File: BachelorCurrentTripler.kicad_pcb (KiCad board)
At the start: 4 copper layers, 81.8 x 81.3 mm, 50 parts, among them J1 Conn_01x07_Pin, J2 Conn_01x01_Pin, J3 Conn_01x01_Pin, J4 Conn_01x04_Socket, J5 Conn_01x01_Pin, Q13 C2M0025120D, Q14 C2M0025120D, Q15 C2M0025120D, Q16 C2M0025120D, Q7 C2M0025120D, Q8 C2M0025120D, U1 STDriveG600, U2 STDriveG600, U3 STDriveG600

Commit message: vias
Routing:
- net /PhaseA/AOUT: track 39.5 -> 47.2 mm
- net GND: track 42.7 -> 45.0 mm, vias 109 -> 105
- net /PhaseC/COUT: track 69.0 -> 66.8 mm
- net Net-(U3-BOOT): track 0.00 -> 2.24 mm
- net /PhaseB/PVCC: track 10.3 -> 11.0 mm

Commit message: local restore changes
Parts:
- C12, C18, C6: value 100u -> 47u; footprint Capacitor_SMD:C_Elec_6.3x7.7 -> easyeda:CAP-SMD_BD6.3-L6.6-W6.6-LS7.3-FD
- C13, C19, C7: footprint Capacitor_SMD:C_Elec_6.3x7.7 -> easyeda:CAP-SMD_BD8.0-L8.3-W8.3-LS9.2-FD-H10.5
- moved C18 1.71 mm to (134.0, 120.5)
- moved C7 1.44 mm to (150.7, 80.0)
- moved C13 1.31 mm to (150.5, 103.5)
- moved C6 0.86 mm to (141.2, 72.8)
- moved C12 0.68 mm to (141.8, 97.6)
- moved R17 0.42 mm to (129.4, 133.0)
- moved R18 0.42 mm to (129.4, 135.5)
- moved C14 0.42 mm to (122.3, 138.5)
- moved C15 0.42 mm to (115.3, 131.5)
- moved R19 0.42 mm to (109.8, 129.5)
- moved C16 0.42 mm to (123.8, 124.0)
- moved C17 0.42 mm to (146.8, 135.5)
- moved Q15 0.42 mm to (138.4, 128.2)
- moved Q16 0.42 mm to (138.4, 135.2)
- moved R14 0.42 mm to (117.1, 138.2)
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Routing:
- net /PhaseA/AOUT: track 47.2 -> 38.8 mm
- net /PhaseB/BOUT: track 47.0 -> 38.7 mm
- net /PhaseC/COUT: track 66.8 -> 58.5 mm
- net +48V: vias 70 -> 134
- added copper zone on In2.Cu, net +12V
- added copper zone on In2.Cu, net +48V
- added copper zone on B.Cu, net GND
- added copper zone on F.Cu, net GND
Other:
- board size 81.8 x 81.3 mm -> 81.8 x 77.8 mm
- board text added: "Stor kondensator mellem 48V og GND men også 12V og GND"
- board text added: "byt"
- board text added: "kør ikke strøm under"

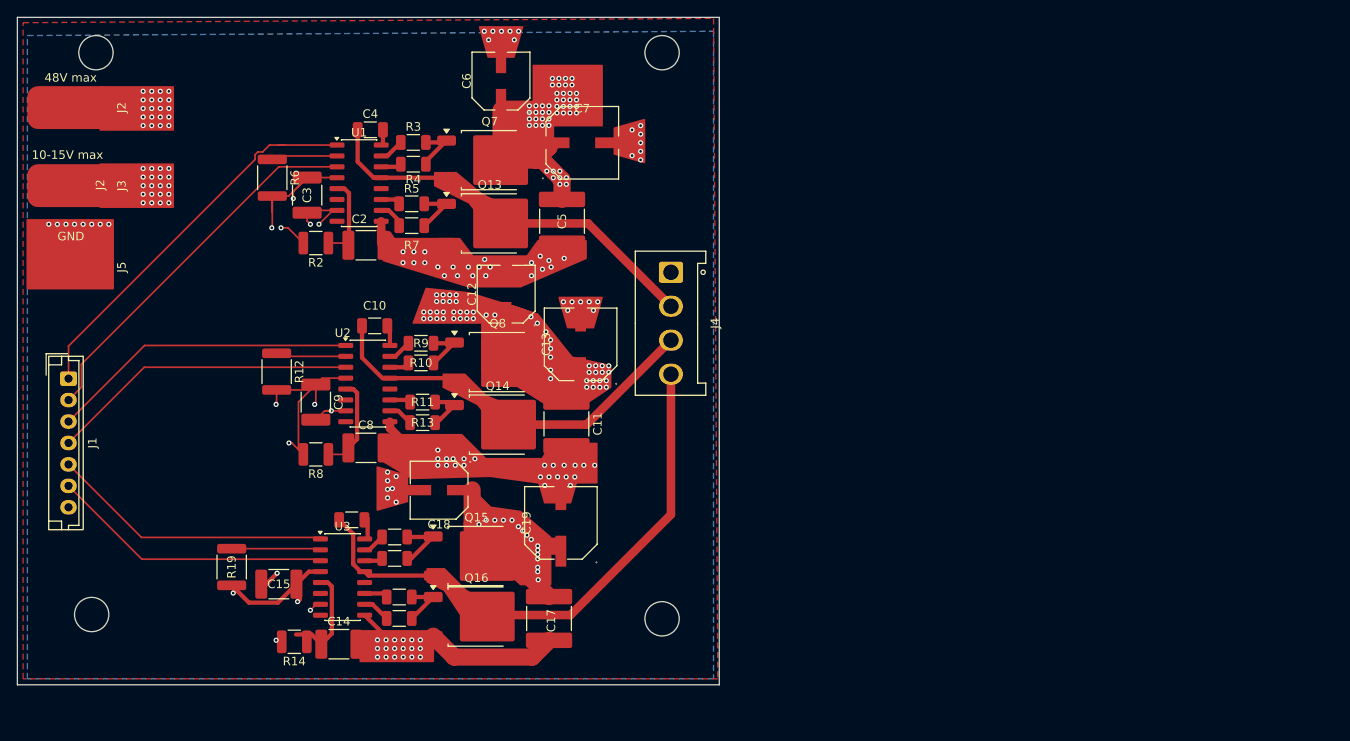
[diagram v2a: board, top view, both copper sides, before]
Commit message: Updates to Secondary side for PCB
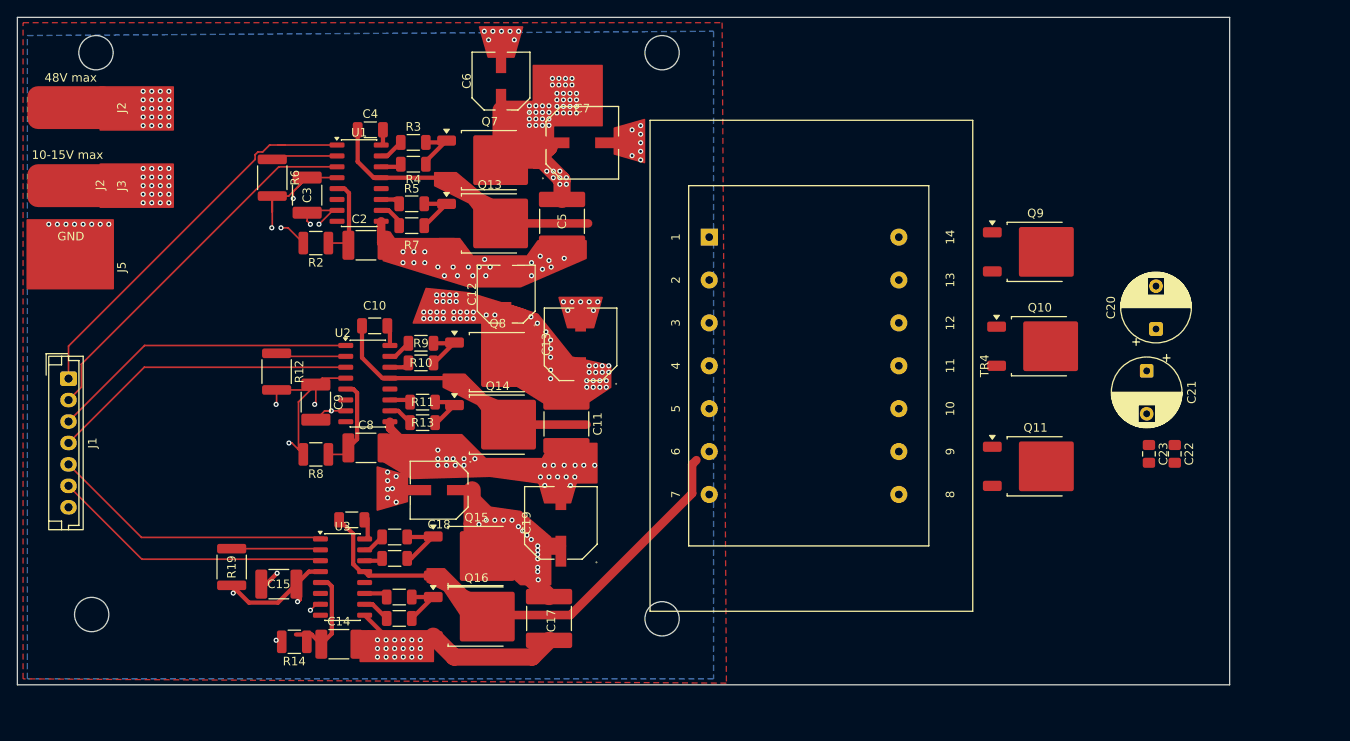
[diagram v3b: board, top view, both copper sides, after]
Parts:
- removed J4: Conn_01x04_Socket, Connector_Hirose:Hirose_DF63M-4P-3.96DSA_1x04_P3.96mm_Vertical
- added C20: 220u, Capacitor_THT:CP_Radial_D8.0mm_P5.00mm, F.Cu at (217.6, 101.7)
- added C21: 100u, Capacitor_THT:CP_Radial_D8.0mm_P5.00mm, F.Cu at (216.5, 106.6)
- added C22: 22u, Capacitor_SMD:C_0805_2012Metric_Pad1.18x1.45mm_HandSolder, F.Cu at (219.8, 116.3)
- added C23: 1u, Capacitor_SMD:C_0805_2012Metric_Pad1.18x1.45mm_HandSolder, F.Cu at (216.8, 116.3)
- added Q10: STD7NK40Z, Package_TO_SOT_SMD:TO-252-2, F.Cu at (204.0, 103.7)
- added Q11: STD7NK40Z, Package_TO_SOT_SMD:TO-252-2, F.Cu at (203.5, 117.7)
- added Q9: STD7NK40Z, Package_TO_SOT_SMD:TO-252-2, F.Cu at (203.5, 92.7)
- added TR4: TEZ16.0-D-1, Transformer_THT:Transformer_Breve_TEZ-47x57, F.Cu at (157.6, 91.0)
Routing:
- net /PhaseB/BOUT: track 38.7 -> 24.8 mm
- net /PhaseA/AOUT: track 38.8 -> 25.2 mm
- net /PhaseC/COUT: track 58.5 -> 49.7 mm
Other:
- board size 81.8 x 77.8 mm -> 141.3 x 77.8 mm

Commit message: all små komponenter er nu 0805, og jeg har fixet strømmen under kondensatorerene, mangler kun at bytte rundt på 12Vin og GND
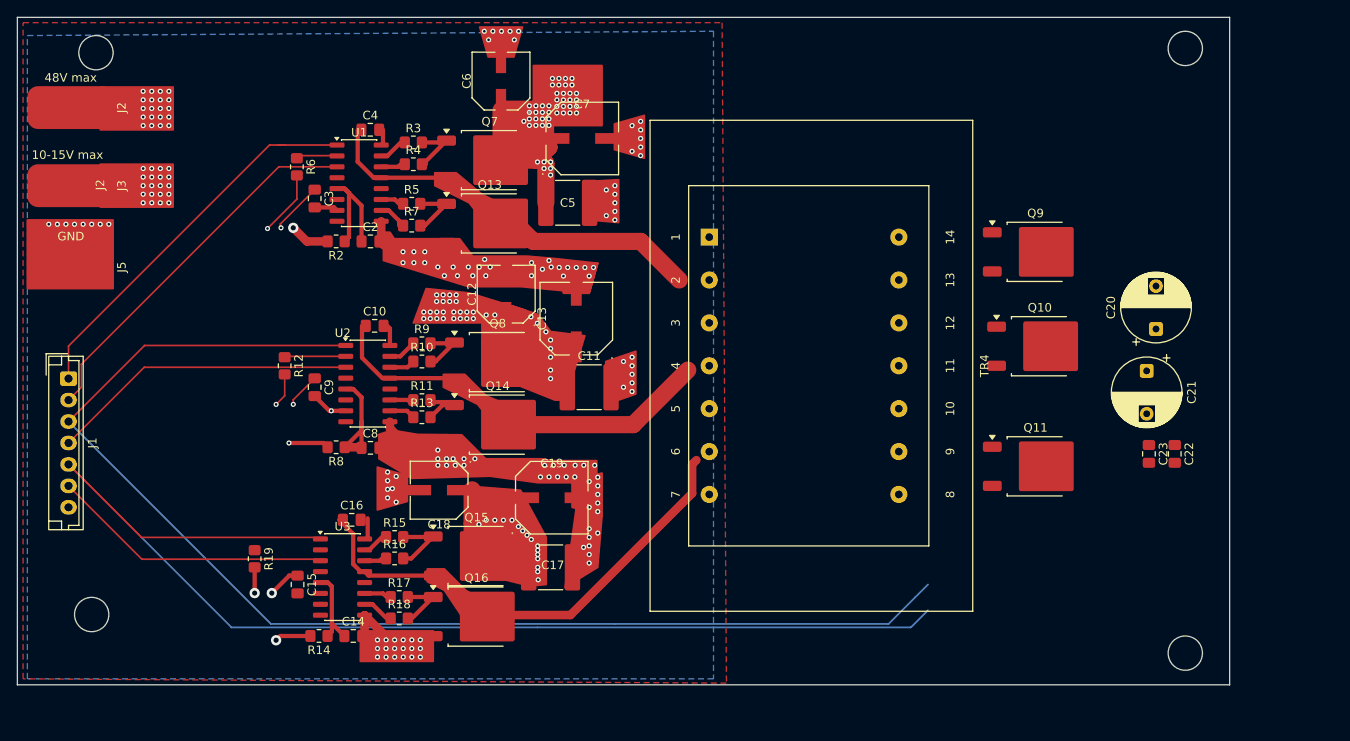
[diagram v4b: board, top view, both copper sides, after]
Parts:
- C10, C16, C4: footprint Capacitor_SMD:C_1206_3216Metric -> Capacitor_SMD:C_0805_2012Metric_Pad1.18x1.45mm_HandSolder
- C14, C15, C2, C3, C8, C9: footprint Capacitor_SMD:C_1812_4532Metric -> Capacitor_SMD:C_0805_2012Metric_Pad1.18x1.45mm_HandSolder
- R10, R11, R13, R15, R16, R17, R18, R3, R4, R5, R7, R9: footprint Resistor_SMD:R_1206_3216Metric -> Resistor_SMD:R_0805_2012Metric_Pad1.20x1.40mm_HandSolder
- R12, R19, R6: footprint Resistor_SMD:R_1812_4532Metric -> Resistor_SMD:R_0805_2012Metric_Pad1.20x1.40mm_HandSolder
- R14, R2, R8: footprint Resistor_SMD:R_1210_3225Metric -> Resistor_SMD:R_0805_2012Metric_Pad1.20x1.40mm_HandSolder
- moved C17 5.96 mm to (147.0, 129.5), turned to 0 degrees
- moved C11 5.03 mm to (151.5, 108.5), turned to 0 degrees
- moved R6 3.14 mm to (117.4, 82.8)
- moved C19 3.12 mm to (147.1, 121.4), turned to 0 degrees
- moved C13 3.04 mm to (150.0, 100.5)
- moved R14 2.96 mm to (120.0, 137.5)
- moved R19 2.85 mm to (112.5, 128.5)
- moved R8 2.51 mm to (122.0, 115.5)
- moved R2 2.37 mm to (122.0, 91.5)
- moved C5 2.25 mm to (149.0, 87.0), turned to 0 degrees
- moved C15 2.18 mm to (117.5, 131.5), turned to -90 degrees
- moved C14 1.93 mm to (124.0, 137.5)
- moved C9 1.74 mm to (119.5, 108.5)
- moved R12 1.16 mm to (116.0, 106.0)
- moved C3 0.97 mm to (119.5, 86.5)
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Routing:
- net /PhaseB/BLIN: track 36.0 -> 147.9 mm
- net /PhaseC/CLIN: track 33.3 -> 142.2 mm
- net +12V: track 180.5 -> 153.4 mm
- net GND: track 45.0 -> 22.0 mm, vias 105 -> 125
- net +48V: track 208.7 -> 192.1 mm, vias 134 -> 117
- net /PhaseB/BOUT: track 24.8 -> 39.2 mm
- net /PhaseA/AOUT: track 25.2 -> 38.5 mm
- net Net-(U3-SD): track 10.4 -> 0.19 mm
- net /PhaseA/PVCC: track 10.2 -> 14.4 mm
- net /PhaseB/PVCC: track 11.0 -> 14.1 mm
- net Net-(U1-SD): track 7.72 -> 4.82 mm
- net /PhaseC/PVCC: track 12.2 -> 9.57 mm
- net Net-(U2-HOFF): track 2.37 -> 3.01 mm
- net Net-(Q8-G): track 6.00 -> 6.63 mm
- net Net-(U2-HON): track 2.79 -> 3.36 mm
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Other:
- outline, holes or cut-outs redrawn

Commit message: nu er vi meget tættere på, den 3 fasede transformer er placeret og interegeret korrekt, sekundær siden er sat, spoler og mosfets, ved ikke om det er det rigtige at gøre men sådan er det jo
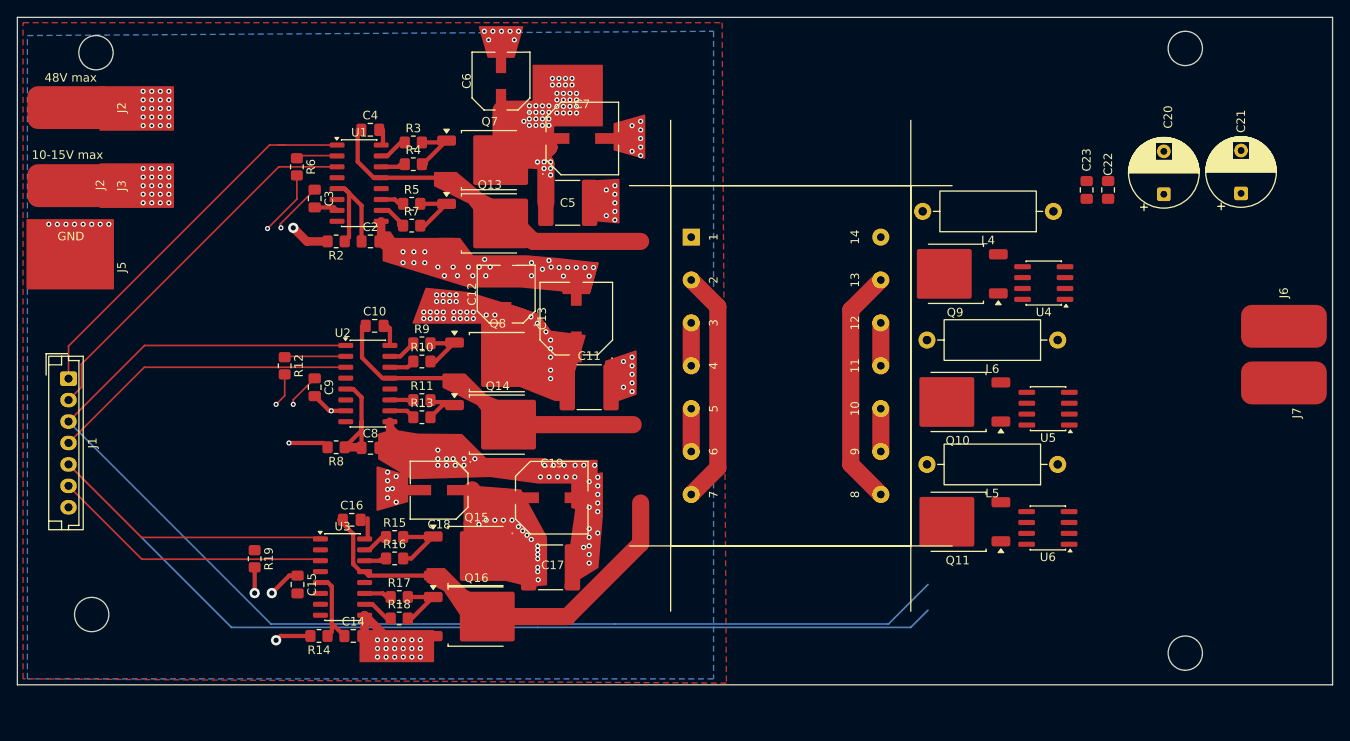
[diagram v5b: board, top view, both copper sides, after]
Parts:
- removed TR4: TEZ16.0-D-1, Transformer_THT:Transformer_Breve_TEZ-47x57
- added J6: Conn_01x01_Pin, Connector_Wire:SolderWirePad_1x01_SMD_5x10mm, F.Cu at (232.5, 101.4)
- added J7: Conn_01x01_Pin, Connector_Wire:SolderWirePad_1x01_SMD_5x10mm, F.Cu at (232.5, 108.0)
- added L4: L, Inductor_THT:L_Axial_L11.0mm_D4.5mm_P15.24mm_Horizontal_Fastron_MECC, F.Cu at (205.6, 88.0)
- added L5: L, Inductor_THT:L_Axial_L11.0mm_D4.5mm_P15.24mm_Horizontal_Fastron_MECC, F.Cu at (206.1, 117.5)
- added L6: L, Inductor_THT:L_Axial_L11.0mm_D4.5mm_P15.24mm_Horizontal_Fastron_MECC, F.Cu at (206.1, 103.0)
- added U4: FAN3268, Package_SO:SOIC-8_3.9x4.9mm_P1.27mm, F.Cu at (204.5, 96.4)
- added U5: FAN3268, Package_SO:SOIC-8_3.9x4.9mm_P1.27mm, F.Cu at (205.0, 111.0)
- added U6: FAN3268, Package_SO:SOIC-8_3.9x4.9mm_P1.27mm, F.Cu at (205.0, 124.9)
- added U7: ~, Transformer_THT:Transformer_Breve_TEZ-47x57, F.Cu at (161.0, 85.0)
- Q10, Q11, Q9: value STD7NK40Z -> IRLR8726EBF
- moved C22 31.7 mm to (212.0, 85.5), turned to 90 degrees
- moved C23 31.6 mm to (209.5, 85.5), turned to 90 degrees
- moved C21 23.4 mm to (227.5, 85.9), turned to 90 degrees
- moved C20 15.7 mm to (218.5, 86.0)
- moved Q10 11.6 mm to (194.5, 110.2), turned to 180 degrees
- moved Q11 11.1 mm to (194.5, 124.2), turned to 180 degrees
- moved Q9 9.72 mm to (194.2, 95.3), turned to 180 degrees
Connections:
- Q10 pad 1: /PhaseB/BLIN -> Net-(Q10-G)
- Q11 pad 1: /PhaseC/CLIN -> Net-(Q11-G)
- Q9 pad 1: /PhaseA/ALin -> Net-(Q9-G)
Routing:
- net /SecondarySide/SecA: track 0.00 -> 27.9 mm
- net /PhaseA/AOUT: track 38.5 -> 59.7 mm
- net /SecondarySide/SecC: track 0.00 -> 5.00 mm
- net /SecondarySide/SecB: track 0.00 -> 5.00 mm
- net /PhaseB/BOUT: track 39.2 -> 35.2 mm
- net /PhaseC/COUT: track 49.7 -> 47.4 mm
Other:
- board size 141.3 x 77.8 mm -> 153.3 x 77.8 mm

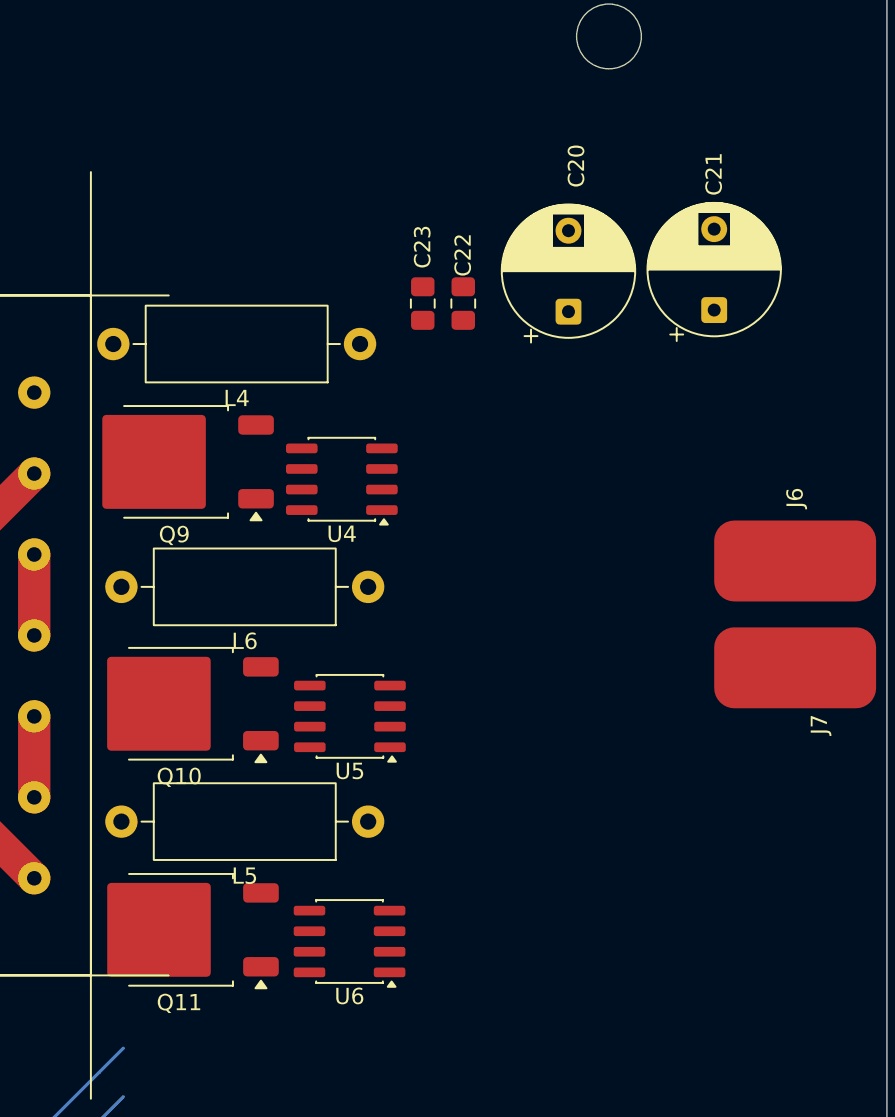
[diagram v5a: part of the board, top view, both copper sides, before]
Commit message: Added resistors and more capacitors
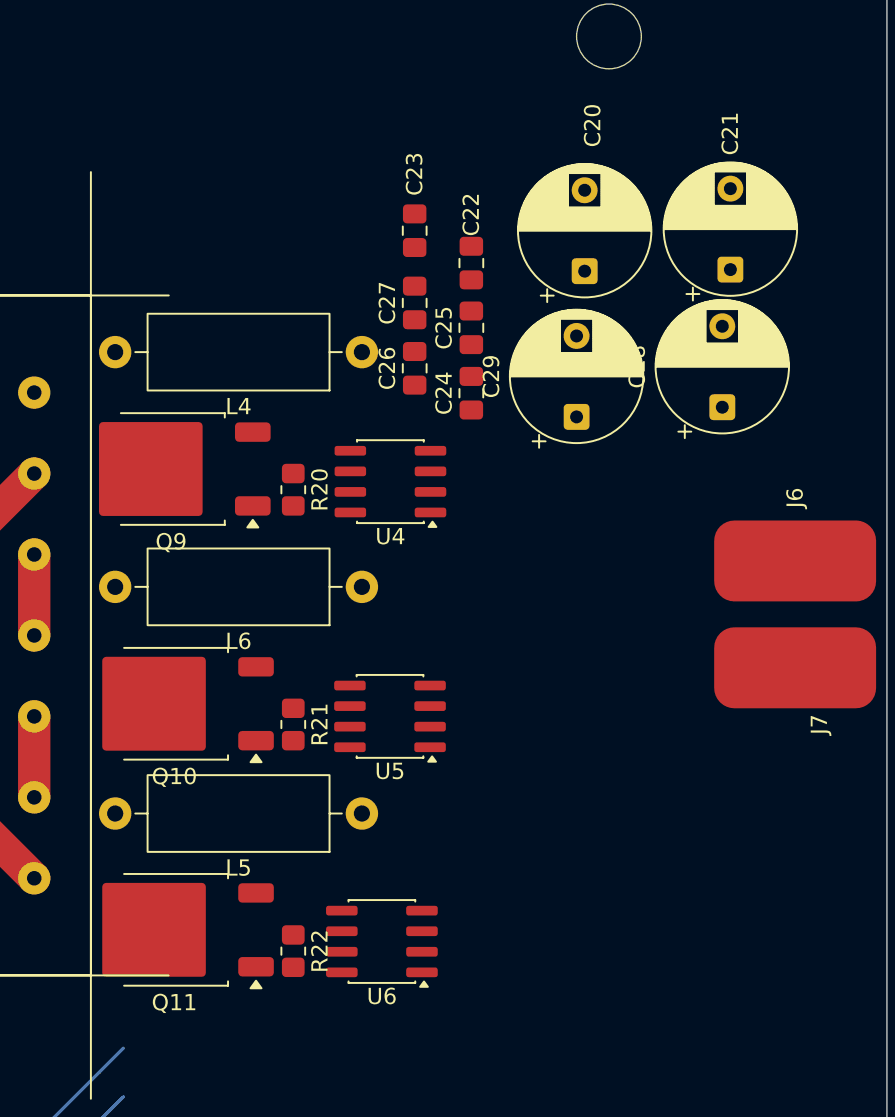
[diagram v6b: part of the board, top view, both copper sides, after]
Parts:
- added C24: 22u, Capacitor_SMD:C_0805_2012Metric_Pad1.18x1.45mm_HandSolder, F.Cu at (212.5, 91.0)
- added C25: 22u, Capacitor_SMD:C_0805_2012Metric_Pad1.18x1.45mm_HandSolder, F.Cu at (212.5, 87.0)
- added C26: 1u, Capacitor_SMD:C_0805_2012Metric_Pad1.18x1.45mm_HandSolder, F.Cu at (209.0, 89.5)
- added C27: 1u, Capacitor_SMD:C_0805_2012Metric_Pad1.18x1.45mm_HandSolder, F.Cu at (209.0, 85.5)
- added C28: 100u, Capacitor_THT:CP_Radial_D8.0mm_P5.00mm, F.Cu at (228.0, 91.9)
- added C29: 220u, Capacitor_THT:CP_Radial_D8.0mm_P5.00mm, F.Cu at (219.0, 92.5)
- added R20: 5m, Resistor_SMD:R_0805_2012Metric_Pad1.20x1.40mm_HandSolder, F.Cu at (201.5, 97.0)
- added R21: 5m, Resistor_SMD:R_0805_2012Metric_Pad1.20x1.40mm_HandSolder, F.Cu at (201.5, 111.5)
- added R22: 5m, Resistor_SMD:R_0805_2012Metric_Pad1.20x1.40mm_HandSolder, F.Cu at (201.5, 125.5)
- moved C23 4.53 mm to (209.0, 81.0)
- moved U4 3.00 mm to (207.5, 96.5)
- moved C20 2.69 mm to (219.5, 83.5)
- moved C21 2.69 mm to (228.5, 83.4)
- moved C22 2.55 mm to (212.5, 83.0)
- moved U5 2.47 mm to (207.5, 111.0)
- moved U6 2.00 mm to (207.0, 124.9)
- moved L5 0.63 mm to (205.7, 117.0)
- moved L4 0.51 mm to (205.7, 88.5)
- moved Q9 0.48 mm to (194.0, 95.7)
- moved L6 0.38 mm to (205.7, 103.0)
- moved Q11 0.31 mm to (194.2, 124.2)
- moved Q10 0.30 mm to (194.2, 110.2)
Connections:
- U4 pad 7: Net-(Q9-G) -> Net-(U4-OUTA)
- U5 pad 7: Net-(Q10-G) -> Net-(U5-OUTA)
- U6 pad 7: Net-(Q11-G) -> Net-(U6-OUTA)
